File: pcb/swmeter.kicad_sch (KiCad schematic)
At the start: 21 parts, among them J1 Conn_Coaxial, J2 AudioPlug, J3_Meter1 Conn_01x02_Male, SW1 SW_DIP_x01, SW2 SW_DIP_x03, U1 LM3914N

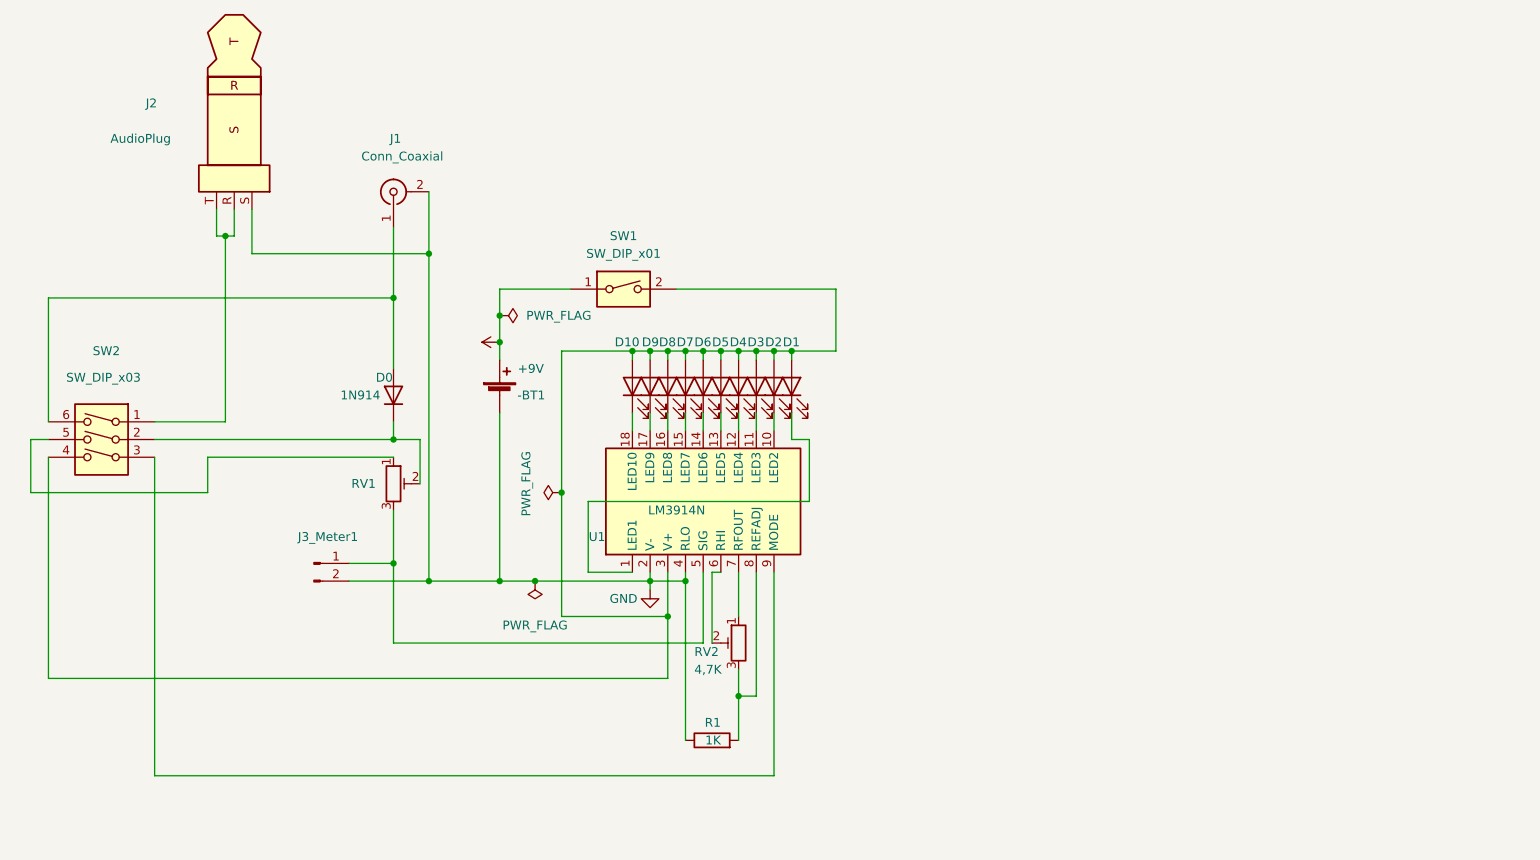
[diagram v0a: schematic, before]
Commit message: design optimizations by adding input switch
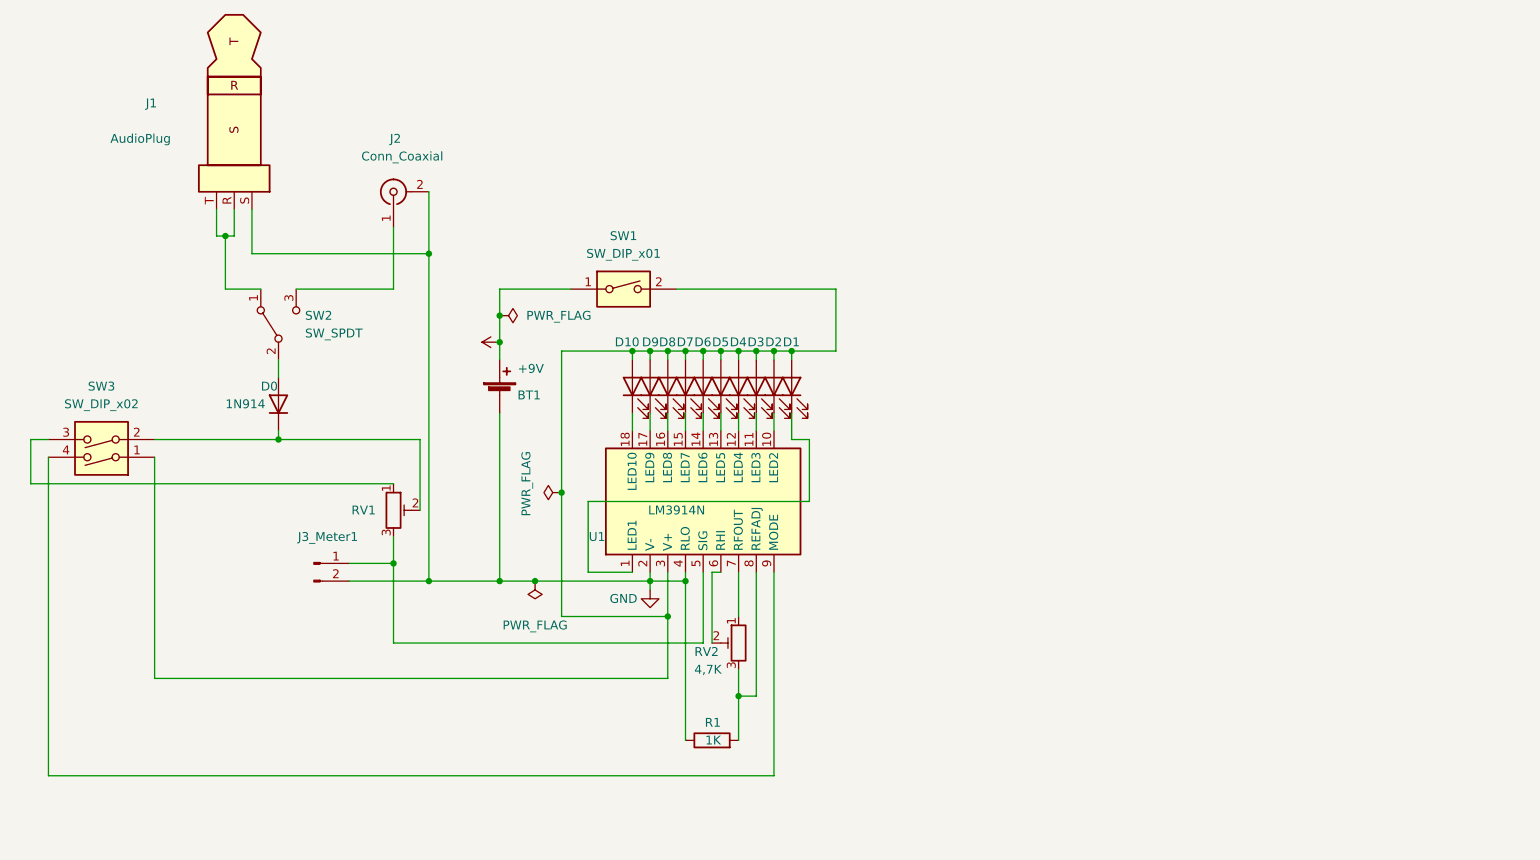
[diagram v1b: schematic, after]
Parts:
- removed SW2: SW_DIP_x03, Button_Switch_THT:SW_DIP_SPSTx03_Slide_6.7x9.18mm_W7.62mm_P2.54mm_LowProfile, symbol Switch:SW_DIP_x03
- added SW2: SW_SPDT, Button_Switch_THT:SW_E-Switch_EG1224_SPDT_Angled, symbol Switch:SW_SPDT
- added SW3: SW_DIP_x02, Button_Switch_THT:SW_DIP_SPSTx02_Slide_6.7x6.64mm_W7.62mm_P2.54mm_LowProfile, symbol Switch:SW_DIP_x02
- renumbered -BT1 to BT1, J2 to J1, J1 to J2
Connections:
- net at D1.2 (A), D10.2 (A), D2.2 (A)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: now also SW3.1
- net at RV1.1: now also SW3.3
- net at D0.1 (K), RV1.2: now also SW3.2
- net at J1.R, J1.T: now also SW2.1 (A)
- net at U1.9 (MODE): now also SW3.4
- net at D0.2 (A): now also SW2.2 (B); no longer J2.1 (In)
- new net: J2.1 (In), SW2.3 (C)
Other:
- moved on the sheet: RV1

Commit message: Opimizations - prettify Silkscreens & Routings - DC-Meter 3-Pin Hheader - Gerber & Layer Files
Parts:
- removed J3_Meter1: Conn_01x02_Male, Connector_PinHeader_1.27mm:PinHeader_1x02_P1.27mm_Vertical, symbol Connector:Conn_01x02_Male
- added J3: Conn_01x03_Female, Connector_PinHeader_1.27mm:PinHeader_1x03_P1.27mm_Vertical, symbol Connector:Conn_01x03_Female
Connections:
- net GND: now also J3.1 (Pin_1)
- net at RV1.3, U1.5 (SIG): now also J3.2 (Pin_2)
- net at D1.2 (A), D10.2 (A), D2.2 (A)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: now also J3.3 (Pin_3)
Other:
- company: (C) WodoWiesel -> © WodoWiesel
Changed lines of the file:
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@@
   (title_block
     (title "SW-Meter")
-    (date "2022-08-23")
-    (rev "0.1")
-    (company "(C) WodoWiesel")
+    (date "2022-10-21")
+    (rev "0.2")
+    (company "© WodoWiesel")
   )
   (junction (at 173.99 90.17) (diameter 0) (color 0 0 0 0)
@@
   (junction (at 168.91 90.17) (diameter 0) (color 0 0 0 0)
   )
+  (junction (at 143.51 118.11) (diameter 0) (color 0 0 0 0)
+  )
   (junction (at 143.51 110.49) (diameter 0) (color 0 0 0 0)
   )
@@
     (stroke (width 0) (type default) (color 0 0 0 0))
   )
-  (wire (pts (xy 113.03 120.65) (xy 119.38 120.65))
+  (wire (pts (xy 111.76 120.65) (xy 119.38 120.65))
     (stroke (width 0) (type default) (color 0 0 0 0))
   )
@@
     (stroke (width 0) (type default) (color 0 0 0 0))
   )
-  (wire (pts (xy 113.03 123.19) (xy 124.46 123.19))
+  (wire (pts (xy 111.76 123.19) (xy 124.46 123.19))
     (stroke (width 0) (type default) (color 0 0 0 0))
   )
@@
     (stroke (width 0) (type default) (color 0 0 0 0))
   )
+  (wire (pts (xy 111.76 118.11) (xy 143.51 118.11))
+    (stroke (width 0) (type default) (color 0 0 0 0))
+  )
   (wire (pts (xy 161.29 123.19) (xy 156.21 123.19))
     (stroke (width 0) (type default) (color 0 0 0 0))
@@
     (stroke (width 0) (type default) (color 0 0 0 0))
   )
-  (wire (pts (xy 143.51 110.49) (xy 143.51 128.27))
+  (wire (pts (xy 143.51 110.49) (xy 143.51 118.11))
     (stroke (width 0) (type default) (color 0 0 0 0))
   )
@@
     (stroke (width 0) (type default) (color 0 0 0 0))
   )
+  (wire (pts (xy 143.51 118.11) (xy 143.51 128.27))
+    (stroke (width 0) (type default) (color 0 0 0 0))
+  )
   (wire (pts (xy 179.07 102.87) (xy 179.07 111.76))
     (stroke (width 0) (type default) (color 0 0 0 0))
@@
   (wire (pts (xy 158.75 128.27) (xy 143.51 128.27))
     (stroke (width 0) (type default) (color 0 0 0 0))
-  )
-  (symbol (lib_id "Connector:Conn_01x02_Male") (at 107.95 120.65 0) (unit 1)
-    (in_bom yes) (on_board yes)
-    (property "Reference" "J3_Meter1" (id 0) (at 114.3 116.84 0)
-      (effects (font (size 1.27 1.27)) (justify right))
-    )
-    (property "Value" "Conn_01x02_Male" (id 1) (at 102.87 114.3 90)
-      (effects (font (size 1.27 1.27)) (justify right) hide)
-    )
-    (property "Footprint" "Connector_PinHeader_1.27mm:PinHeader_1x02_P1.27mm_Vertical" (id 2) (at 107.95 120.65 0)
-      (effects (font (size 1.27 1.27)) hide)
-    )
-    (property "Datasheet" "~" (id 3) (at 107.95 120.65 0)
-      (effects (font (size 1.27 1.27)) hide)
-    )
-    (pin "1")
-    (pin "2")
   )
   (symbol (lib_id "power:+9V") (at 134.62 88.9 90) (unit 1)
@@
     )
     (pin "1")
+  )
+  (symbol (lib_id "Connector:Conn_01x03_Female") (at 106.68 120.65 180) (unit 1)
+    (in_bom yes) (on_board yes)
+    (property "Reference" "J3" (id 0) (at 104.14 120.65 0))
+    (property "Value" "Conn_01x03_Female" (id 1) (at 107.315 115.57 0)
+      (effects (font (size 1.27 1.27)) hide)
+    )
+    (property "Footprint" "Connector_PinHeader_1.27mm:PinHeader_1x03_P1.27mm_Vertical" (id 2) (at 106.68 120.65 0)
+      (effects (font (size 1.27 1.27)) hide)
+    )
+    (property "Datasheet" "~" (id 3) (at 106.68 120.65 0)
+      (effects (font (size 1.27 1.27)) hide)
+    )
+    (pin "1")
+    (pin "2")
+    (pin "3")
   )
   (symbol (lib_id "Device:LED") (at 176.53 95.25 90) (unit 1)
@@
       (reference "J2") (unit 1) (value "Conn_Coaxial") (footprint "Connector_Coaxial:BNC_TEConnectivity_1478035_Horizontal")
     )
-    (path "/18c49140-b050-4127-a72e-9184b4bc32d5"
-      (reference "J3_Meter1") (unit 1) (value "Conn_01x02_Male") (footprint "Connector_PinHeader_1.27mm:PinHeader_1x02_P1.27mm_Vertical")
+    (path "/1da93d0b-7ffa-4107-a474-9c3680373a84"
+      (reference "J3") (unit 1) (value "Conn_01x03_Female") (footprint "Connector_PinHeader_1.27mm:PinHeader_1x03_P1.27mm_Vertical")
     )
     (path "/c6c532ae-3b84-4e0c-90e3-cd79bbcec0ea"

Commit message: export update
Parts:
- added CV1: (no value), Capacitor_THT:CP_Radial_D5.0mm_P2.50mm, symbol Device:C_Trim_Small
- R1: value 1K -> 330Ω
- RV1: value R_Potentiometer_Trim -> 4,7kΩ
- RV2: value 4,7K -> 4,7kΩ
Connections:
- net GND: now also CV1.2
- net at D1.2 (A), D10.2 (A), D2.2 (A)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: now also CV1.1

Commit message: -double trace width -use 2 same switches -add recycling logo -add HASL info -optimize gnd-plane
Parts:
- removed SW1: SW_DIP_x01, Button_Switch_THT:SW_DIP_SPSTx01_Slide_9.78x4.72mm_W7.62mm_P2.54mm, symbol Switch:SW_DIP_x01
- added SW1: SW_SPDT, Button_Switch_THT:SW_E-Switch_EG1224_SPDT_Angled, symbol Switch:SW_SPDT
- CV1: value (none) -> 22µF
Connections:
- net +9V: now also SW1.2 (B)
- net at CV1.1, D1.2 (A), D10.2 (A)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: now also SW1.1 (A)
- no-connect marks 0 -> 1
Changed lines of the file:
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@@
   (title_block
     (title "SW-Meter")
-    (date "2022-11-07")
+    (date "2022-11-15")
     (rev "0.2")
     (company "© WodoWiesel")
@@
   (junction (at 163.83 90.17) (diameter 0) (color 0 0 0 0)
   )
+  (no_connect (at 156.21 83.82))
   (wire (pts (xy 156.21 90.17) (xy 158.75 90.17))
     (stroke (width 0) (type default) (color 0 0 0 0))
@@
     (stroke (width 0) (type default) (color 0 0 0 0))
   )
-  (wire (pts (xy 160.02 81.28) (xy 182.88 81.28))
+  (wire (pts (xy 156.21 81.28) (xy 182.88 81.28))
     (stroke (width 0) (type default) (color 0 0 0 0))
   )
@@
     (stroke (width 0) (type default) (color 0 0 0 0))
   )
-  (wire (pts (xy 134.62 81.28) (xy 144.78 81.28))
+  (wire (pts (xy 134.62 81.28) (xy 146.05 81.28))
     (stroke (width 0) (type default) (color 0 0 0 0))
   )
@@
     (stroke (width 0) (type default) (color 0 0 0 0))
   )
+  (wire (pts (xy 156.21 81.28) (xy 156.21 78.74))
+    (stroke (width 0) (type default) (color 0 0 0 0))
+  )
   (wire (pts (xy 153.67 90.17) (xy 156.21 90.17))
     (stroke (width 0) (type default) (color 0 0 0 0))
@@
   (wire (pts (xy 163.83 121.92) (xy 163.83 134.62))
     (stroke (width 0) (type default) (color 0 0 0 0))
+  )
+  (symbol (lib_id "Switch:SW_SPDT") (at 151.13 81.28 0) (unit 1)
+    (in_bom yes) (on_board yes) (fields_autoplaced)
+    (property "Reference" "SW1" (id 0) (at 151.13 73.66 0))
+    (property "Value" "SW_SPDT" (id 1) (at 151.13 76.2 0))
+    (property "Footprint" "Button_Switch_THT:SW_E-Switch_EG1224_SPDT_Angled" (id 2) (at 151.13 81.28 0)
+      (effects (font (size 1.27 1.27)) hide)
+    )
+    (property "Datasheet" "~" (id 3) (at 151.13 81.28 0)
+      (effects (font (size 1.27 1.27)) hide)
+    )
+    (pin "1")
+    (pin "2")
+    (pin "3")
   )
   (symbol (lib_id "power:+9V") (at 134.62 88.9 90) (unit 1)
@@
     (pin "2")
   )
-  (symbol (lib_id "Switch:SW_DIP_x01") (at 152.4 81.28 0) (unit 1)
-    (in_bom yes) (on_board yes) (fields_autoplaced)
-    (property "Reference" "SW1" (id 0) (at 152.4 73.66 0))
-    (property "Value" "SW_DIP_x01" (id 1) (at 152.4 76.2 0))
-    (property "Footprint" "Button_Switch_THT:SW_DIP_SPSTx01_Slide_9.78x4.72mm_W7.62mm_P2.54mm" (id 2) (at 152.4 81.28 0)
-      (effects (font (size 1.27 1.27)) hide)
-    )
-    (property "Datasheet" "~" (id 3) (at 152.4 81.28 0)
-      (effects (font (size 1.27 1.27)) hide)
-    )
-    (pin "1")
-    (pin "2")
-  )
   (symbol (lib_id "Switch:SW_DIP_x02") (at 77.47 102.87 180) (unit 1)
     (in_bom yes) (on_board yes) (fields_autoplaced)
@@
       (effects (font (size 1.27 1.27)) (justify left))
     )
-    (property "Value" "" (id 1) (at 152.4 133.35 0)
+    (property "Value" "22µF" (id 1) (at 152.4 133.35 0)
       (effects (font (size 1.27 1.27)) (justify left))
     )
@@
       (reference "RV2") (unit 1) (value "4,7kΩ") (footprint "Potentiometer_THT:Potentiometer_Bourns_3266Y_Vertical")
     )
-    (path "/9b9c9f2d-c3f0-4093-8f37-35fad5b79e40"
-      (reference "SW1") (unit 1) (value "SW_DIP_x01") (footprint "Button_Switch_THT:SW_DIP_SPSTx01_Slide_9.78x4.72mm_W7.62mm_P2.54mm")
+    (path "/0feb073a-d146-4a2d-9dc2-336bf04c0922"
+      (reference "SW1") (unit 1) (value "SW_SPDT") (footprint "Button_Switch_THT:SW_E-Switch_EG1224_SPDT_Angled")
     )
     (path "/413dad84-3a3c-41c6-8962-39b45afd056c"

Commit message: update v0.4
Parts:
- removed BT1: Battery_Cell, Battery:BatteryHolder_Eagle_12BH611-GR, symbol Device:Battery_Cell
- removed CV1: 22µF, Capacitor_THT:CP_Radial_D5.0mm_P2.50mm, symbol Device:C_Trim_Small
- added C1: 22µf, Capacitor_THT:CP_Radial_D5.0mm_P2.50mm, symbol Device:C_Polarized
- added J0: (no value), Connector_PinHeader_2.54mm:PinHeader_1x02_P2.54mm_Vertical, symbol Connector:Conn_01x02_Female
- renumbered D2 to D10, D10 to D2, D9 to D3, D8 to D4, D7 to D5, D5 to D7, D4 to D8, D3 to D9
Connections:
- net +9V: now also J0.2 (Pin_2)
- net GND: now also SW3.3, C1.2, J0.1 (Pin_1)
- net at D1.2 (A), D10.2 (A), D2.2 (A)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: now also C1.1
- net at RV1.1: now also SW3.2; no longer SW3.3
- net at D0.1 (K), RV1.2: no longer SW3.2
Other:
- moved on the sheet: D1, RV1

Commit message: improve readability
improve readability
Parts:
- C1: value 22µf -> (none)
- J0: value (none) -> Conn_01x02_Female
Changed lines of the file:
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@@
     (in_bom yes) (on_board yes)
     (property "Reference" "J0" (id 0) (at 130.175 87.63 0))
-    (property "Value" "" (id 1) (at 127 95.25 90)
+    (property "Value" "Conn_01x02_Female" (id 1) (at 127 95.25 90)
       (effects (font (size 1.27 1.27)) hide)
     )
@@
     (pin "1")
   )
-  (symbol (lib_id "power:GND") (at 156.21 124.46 0) (unit 1)
+  (symbol (lib_name "GND_1") (lib_id "power:GND") (at 156.21 124.46 0) (unit 1)
     (in_bom yes) (on_board yes)
     (property "Reference" "#PWR02" (id 0) (at 156.21 130.81 0)
@@
       (effects (font (size 1.27 1.27)) (justify right))
     )
-    (property "Value" "22µf" (id 1) (at 144.78 132.08 0)
+    (property "Value" "" (id 1) (at 144.78 132.08 0)
       (effects (font (size 1.27 1.27)) (justify right))
     )
@@
     )
     (path "/f2b0acb5-9834-4e4e-bea0-9465491ec191"
-      (reference "C1") (unit 1) (value "22µf") (footprint "Capacitor_THT:CP_Radial_D5.0mm_P2.50mm")
+      (reference "C1") (unit 1) (value "22µF") (footprint "Capacitor_THT:CP_Radial_D5.0mm_P2.50mm")
     )
     (path "/63cc9df1-9971-4009-89ca-7fdaf2479f3f"
